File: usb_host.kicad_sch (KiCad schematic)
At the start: 10 parts, among them J10 USB_A, U10 TPS2051BDBVR, U11 RCLAMP0504F.TCT

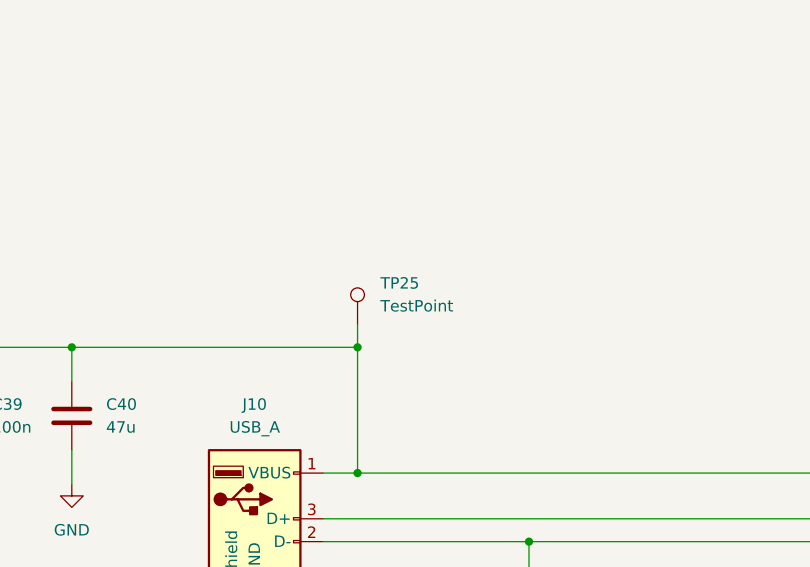
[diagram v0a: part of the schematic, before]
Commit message: feat: add board dimensions and change mcu position
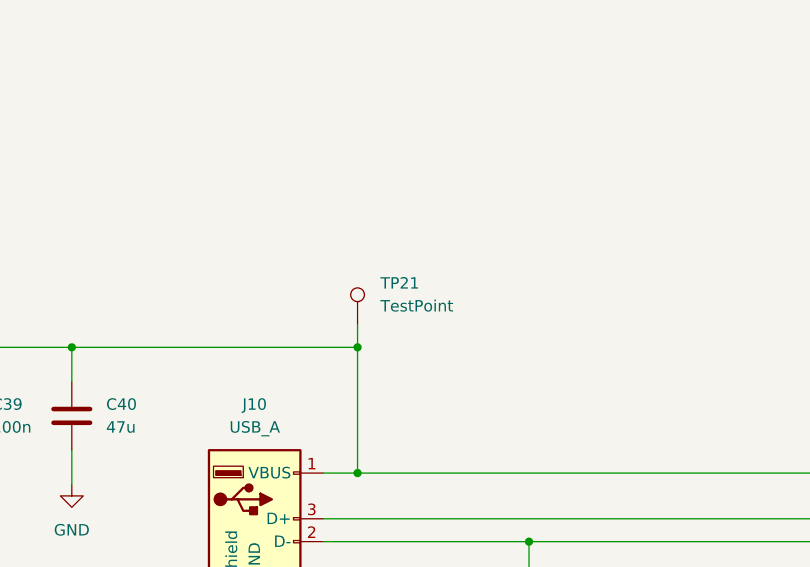
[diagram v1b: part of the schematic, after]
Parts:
- renumbered TP25 to TP21
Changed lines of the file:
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@@
 		(dnp no)
 		(fields_autoplaced yes)
-		(property "Reference" "TP25"
+		(property "Reference" "TP21"
 			(at 186.69 55.1179 0)
 			(show_name no)
@@
 			(project "reflow_station"
 				(path "/77770e37-dda2-4cf3-b2f1-cea4793bc3be/93249a2a-e51b-4c44-9b6d-4c6bfcead48b/b56b01c8-a4d6-4add-b4c8-1a1bd46e73bf"
-					(reference "TP25")
+					(reference "TP21")
 					(unit 1)
 				)

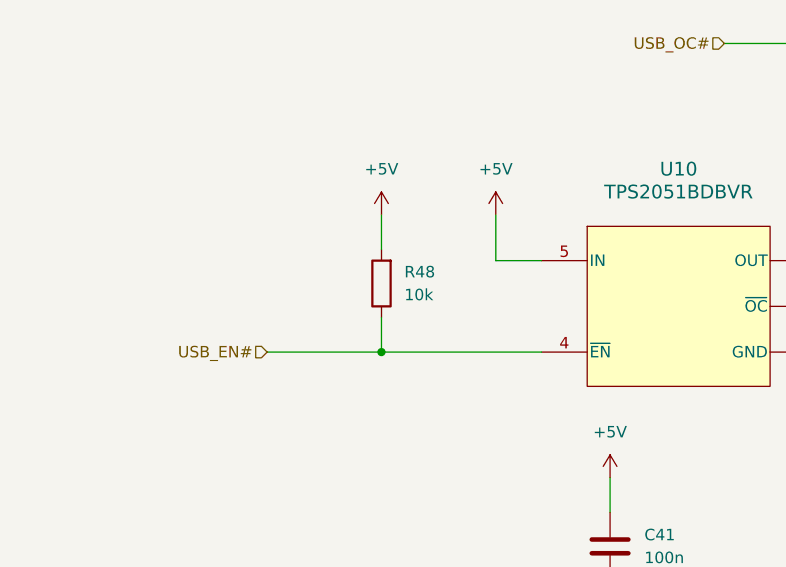
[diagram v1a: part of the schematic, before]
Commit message: feat: route config switches and SWD debug
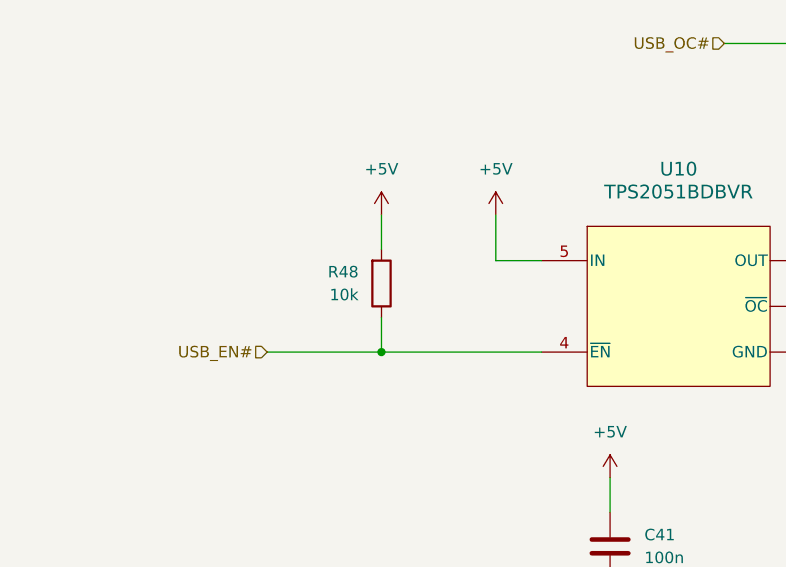
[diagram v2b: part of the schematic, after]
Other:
- moved on the sheet: R48
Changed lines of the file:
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@@
 	(symbol
 		(lib_id "reflow_station_symbols:R")
-		(at 63.5 78.74 180)
+		(at 63.5 78.74 0)
+		(mirror x)
 		(unit 1)
 		(body_style 1)
@@
 		(in_pos_files yes)
 		(dnp no)
-		(fields_autoplaced yes)
 		(property "Reference" "R48"
-			(at 66.04 77.4699 0)
+			(at 60.96 77.4699 0)
 			(show_name no)
 			(do_not_autoplace no)
@@
 		)
 		(property "Value" "10k"
-			(at 66.04 80.0099 0)
+			(at 60.96 80.0099 0)
 			(show_name no)
 			(do_not_autoplace no)
@@
 		)
 		(property "Footprint" "reflow_station_library:R_0402_1005Metric"
-			(at 65.278 78.74 90)
+			(at 61.722 78.74 90)
 			(hide yes)
 			(show_name no)

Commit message: feat: route remaining traces
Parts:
- renumbered R47 to R53, R48 to R54
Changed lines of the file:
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@@
 		(dnp no)
 		(fields_autoplaced yes)
-		(property "Reference" "#PWR0102"
+		(property "Reference" "#PWR0103"
 			(at 175.26 124.46 0)
 			(hide yes)
@@
 			(project "reflow_station"
 				(path "/77770e37-dda2-4cf3-b2f1-cea4793bc3be/93249a2a-e51b-4c44-9b6d-4c6bfcead48b/b56b01c8-a4d6-4add-b4c8-1a1bd46e73bf"
-					(reference "#PWR0102")
+					(reference "#PWR0103")
 					(unit 1)
 				)
@@
 		(dnp no)
 		(fields_autoplaced yes)
-		(property "Reference" "#PWR095"
+		(property "Reference" "#PWR096"
 			(at 139.7 83.82 0)
 			(hide yes)
@@
 			(project "reflow_station"
 				(path "/77770e37-dda2-4cf3-b2f1-cea4793bc3be/93249a2a-e51b-4c44-9b6d-4c6bfcead48b/b56b01c8-a4d6-4add-b4c8-1a1bd46e73bf"
-					(reference "#PWR095")
+					(reference "#PWR096")
 					(unit 1)
 				)
@@
 		(in_pos_files yes)
 		(dnp no)
-		(property "Reference" "R48"
+		(property "Reference" "R54"
 			(at 60.96 77.4699 0)
 			(show_name no)
@@
 			(project "reflow_station"
 				(path "/77770e37-dda2-4cf3-b2f1-cea4793bc3be/93249a2a-e51b-4c44-9b6d-4c6bfcead48b/b56b01c8-a4d6-4add-b4c8-1a1bd46e73bf"
-					(reference "R48")
+					(reference "R54")
 					(unit 1)
 				)
@@
 		(dnp no)
 		(fields_autoplaced yes)
-		(property "Reference" "#PWR097"
+		(property "Reference" "#PWR098"
 			(at 115.57 97.79 0)
 			(hide yes)
@@
 			(project "reflow_station"
 				(path "/77770e37-dda2-4cf3-b2f1-cea4793bc3be/93249a2a-e51b-4c44-9b6d-4c6bfcead48b/b56b01c8-a4d6-4add-b4c8-1a1bd46e73bf"
-					(reference "#PWR097")
+					(reference "#PWR098")
 					(unit 1)
 				)
@@
 		(dnp no)
 		(fields_autoplaced yes)
-		(property "Reference" "#PWR098"
+		(property "Reference" "#PWR099"
 			(at 172.72 105.41 0)
 			(hide yes)
@@
 			(project "reflow_station"
 				(path "/77770e37-dda2-4cf3-b2f1-cea4793bc3be/93249a2a-e51b-4c44-9b6d-4c6bfcead48b/b56b01c8-a4d6-4add-b4c8-1a1bd46e73bf"
-					(reference "#PWR098")
+					(reference "#PWR099")
 					(unit 1)
 				)
@@
 		(dnp no)
 		(fields_autoplaced yes)
-		(property "Reference" "#PWR0101"
+		(property "Reference" "#PWR0102"
 			(at 152.4 124.46 0)
 			(hide yes)
@@
 			(project "reflow_station"
 				(path "/77770e37-dda2-4cf3-b2f1-cea4793bc3be/93249a2a-e51b-4c44-9b6d-4c6bfcead48b/b56b01c8-a4d6-4add-b4c8-1a1bd46e73bf"
-					(reference "#PWR0101")
+					(reference "#PWR0102")
 					(unit 1)
 				)
@@
 		(dnp no)
 		(fields_autoplaced yes)
-		(property "Reference" "#PWR093"
+		(property "Reference" "#PWR094"
 			(at 63.5 74.93 0)
 			(hide yes)
@@
 			(project "reflow_station"
 				(path "/77770e37-dda2-4cf3-b2f1-cea4793bc3be/93249a2a-e51b-4c44-9b6d-4c6bfcead48b/b56b01c8-a4d6-4add-b4c8-1a1bd46e73bf"
-					(reference "#PWR093")
+					(reference "#PWR094")
 					(unit 1)
 				)
@@
 		(dnp no)
 		(fields_autoplaced yes)
-		(property "Reference" "#PWR099"
+		(property "Reference" "#PWR0100"
 			(at 88.9 104.14 0)
 			(hide yes)
@@
 			(project "reflow_station"
 				(path "/77770e37-dda2-4cf3-b2f1-cea4793bc3be/93249a2a-e51b-4c44-9b6d-4c6bfcead48b/b56b01c8-a4d6-4add-b4c8-1a1bd46e73bf"
-					(reference "#PWR099")
+					(reference "#PWR0100")
 					(unit 1)
 				)
@@
 		(dnp no)
 		(fields_autoplaced yes)
-		(property "Reference" "#PWR092"
+		(property "Reference" "#PWR093"
 			(at 114.3 41.91 0)
 			(hide yes)
@@
 			(project "reflow_station"
 				(path "/77770e37-dda2-4cf3-b2f1-cea4793bc3be/93249a2a-e51b-4c44-9b6d-4c6bfcead48b/b56b01c8-a4d6-4add-b4c8-1a1bd46e73bf"
-					(reference "#PWR092")
+					(reference "#PWR093")
 					(unit 1)
 				)
@@
 		(dnp no)
 		(fields_autoplaced yes)
-		(property "Reference" "#PWR096"
+		(property "Reference" "#PWR097"
 			(at 152.4 83.82 0)
 			(hide yes)
@@
 			(project "reflow_station"
 				(path "/77770e37-dda2-4cf3-b2f1-cea4793bc3be/93249a2a-e51b-4c44-9b6d-4c6bfcead48b/b56b01c8-a4d6-4add-b4c8-1a1bd46e73bf"
-					(reference "#PWR096")
+					(reference "#PWR097")
 					(unit 1)
 				)
@@
 		(dnp no)
 		(fields_autoplaced yes)
-		(property "Reference" "#PWR094"
+		(property "Reference" "#PWR095"
 			(at 76.2 74.93 0)
 			(hide yes)
@@
 			(project "reflow_station"
 				(path "/77770e37-dda2-4cf3-b2f1-cea4793bc3be/93249a2a-e51b-4c44-9b6d-4c6bfcead48b/b56b01c8-a4d6-4add-b4c8-1a1bd46e73bf"
-					(reference "#PWR094")
+					(reference "#PWR095")
 					(unit 1)
 				)
@@
 		(dnp no)
 		(fields_autoplaced yes)
-		(property "Reference" "#PWR0100"
+		(property "Reference" "#PWR0101"
 			(at 88.9 121.92 0)
 			(hide yes)
@@
 			(project "reflow_station"
 				(path "/77770e37-dda2-4cf3-b2f1-cea4793bc3be/93249a2a-e51b-4c44-9b6d-4c6bfcead48b/b56b01c8-a4d6-4add-b4c8-1a1bd46e73bf"
-					(reference "#PWR0100")
+					(reference "#PWR0101")
 					(unit 1)
 				)
@@
 		(dnp no)
 		(fields_autoplaced yes)
-		(property "Reference" "R47"
+		(property "Reference" "R53"
 			(at 116.84 44.4499 0)
 			(show_name no)
@@
 			(project "reflow_station"
 				(path "/77770e37-dda2-4cf3-b2f1-cea4793bc3be/93249a2a-e51b-4c44-9b6d-4c6bfcead48b/b56b01c8-a4d6-4add-b4c8-1a1bd46e73bf"
-					(reference "R47")
+					(reference "R53")
 					(unit 1)
 				)
